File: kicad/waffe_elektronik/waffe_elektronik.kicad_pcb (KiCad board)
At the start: 4 copper layers, 59.6 x 55 mm, 86 parts, among them J1 WS2812 HP-Streifen, J2 GX16 7-polig, J3 USB-C (Flashen + Laden), J4 OLED I²C (Qwiic), J5 Drehgeber, J6 IR-LED + TSOP 6, J7 TF-018, J8 Abzug + Nachladen, M1 Vibromotor, Q1 AO3400A, Q2 AO3400A, Q3 FS8205A, Q4 2N7002, SW3 RESET, SW4 BOOT, U1 IP5306-I2C, U12 USBLC6-2SC6, U14 ZD35Q1GC-IB, U15 DW01A, U2 AMS1117-3.3, U4 ESP32-S3-WROOM-1-N16R8, U6 MAX98357A

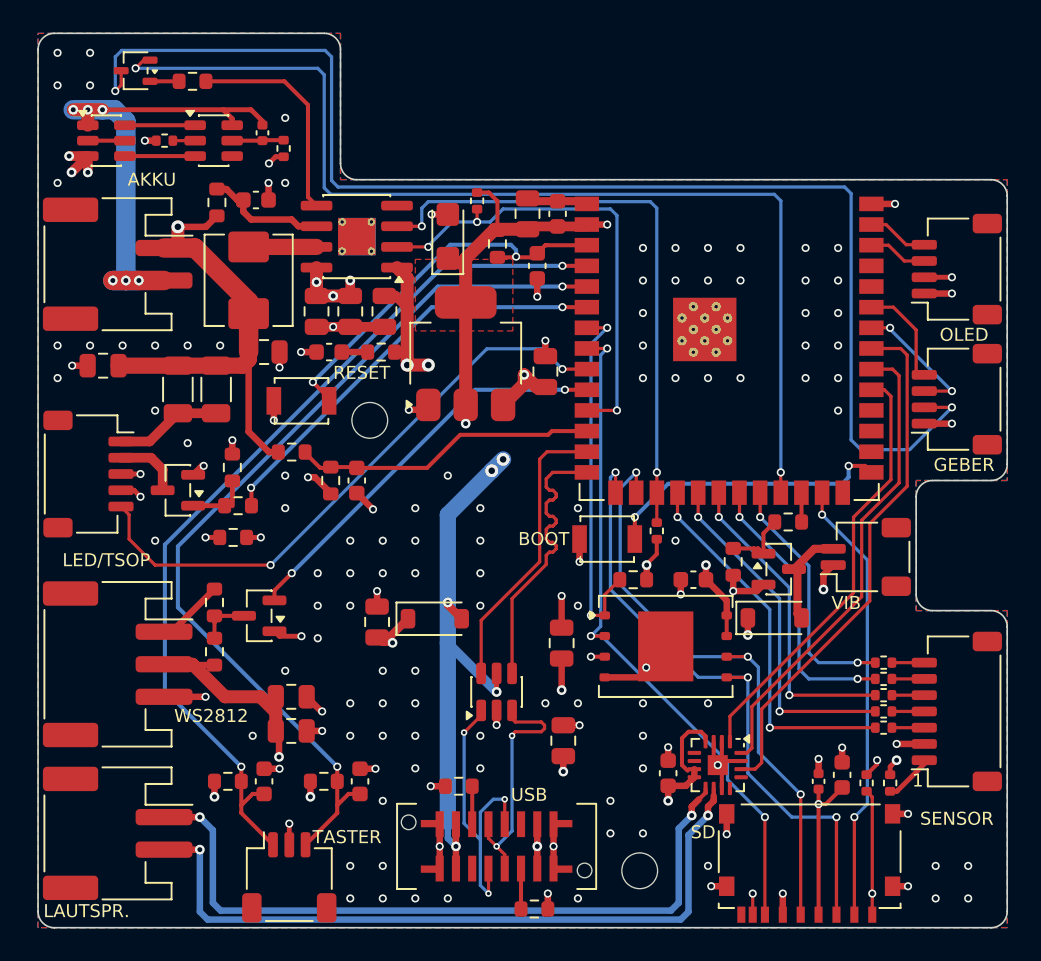
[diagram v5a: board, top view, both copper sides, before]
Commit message: Platine: Lastschalter TPS22810 hinter dem IP5306 (EN = IRQ), RESET in die Lasche, Dämpfung an der USB-Buchse
Co-Authored-By: Claude Opus 5.5 <noreply@anthropic.com>
Claude-Session: https://claude.ai/code/session_01KkZzubjLKyW9odUwvmxTog
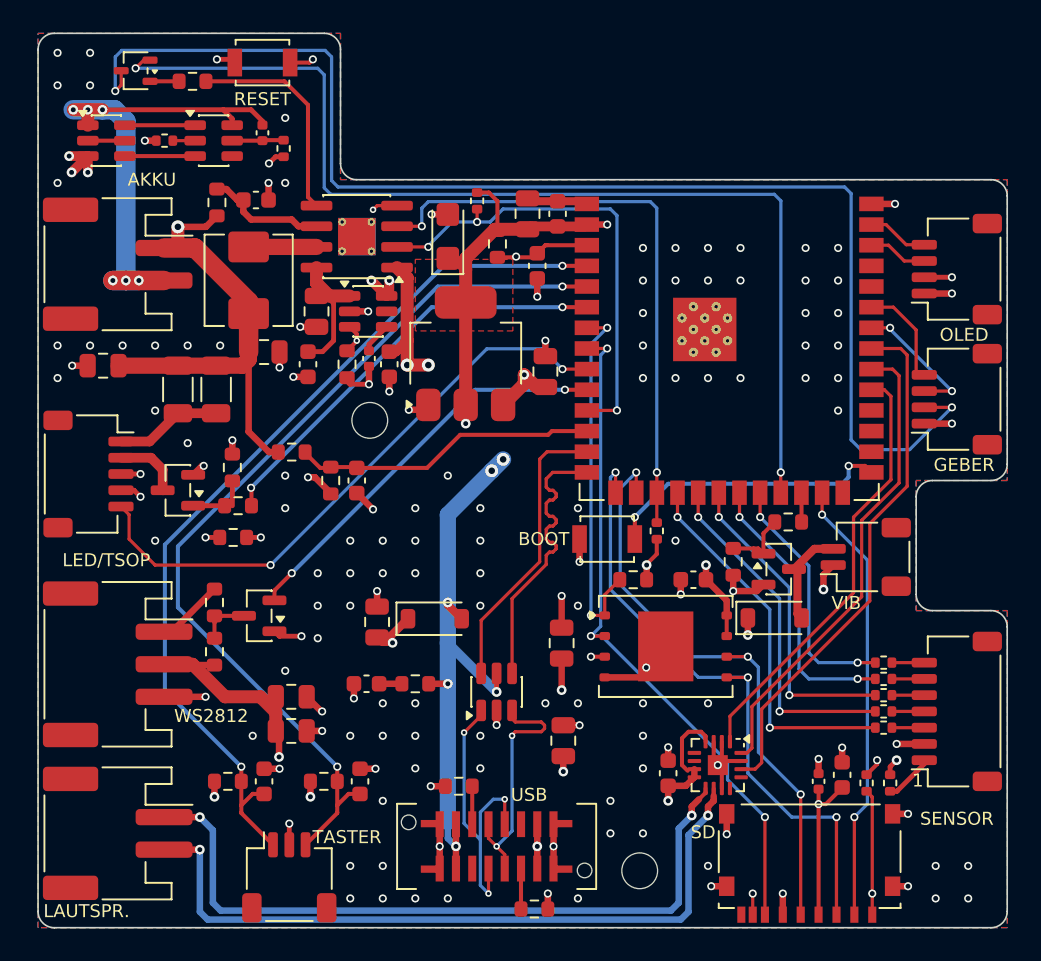
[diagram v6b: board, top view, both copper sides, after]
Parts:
- added C33: 10n, Capacitor_SMD:C_0402_1005Metric, F.Cu at (20.4, 11.0)
- added R42: 100k, Resistor_SMD:R_0603_1608Metric, F.Cu at (19.0, 11.3)
- added U16: TPS22810, Package_TO_SOT_SMD:SOT-23-6, F.Cu at (20.3, 8.10)
- C30: value 22u -> 10u; footprint Capacitor_SMD:C_0805_2012Metric -> Capacitor_SMD:C_0603_1608Metric
- C4: footprint Capacitor_SMD:C_0805_2012Metric -> Capacitor_SMD:C_0603_1608Metric
- moved SW3 20.9 mm to (13.8, -7.20)
- moved C29 20.5 mm to (20.2, 31.0)
- moved R1 20.5 mm to (23.2, 31.0)
- moved C30 4.16 mm to (16.6, 11.3)
- moved C4 3.26 mm to (21.6, 11.3)
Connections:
- C20 pad 1: 5V_PERIPH -> Net-(U1-VOUT)
- C30 pad 1: 5V_PERIPH -> Net-(U1-VOUT)
- U1 pad 4: unconnected-(U1-LED3-Pad4) -> IP_IRQ
- U1 pad 8: 5V_PERIPH -> Net-(U1-VOUT)
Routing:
- net IP_IRQ: track 0.00 -> 12.3 mm, vias 0 -> 2
- net Net-(U1-VOUT): track 0.00 -> 8.11 mm
- net Net-(U4-EN): track 23.9 -> 31.5 mm
- net 5V_PERIPH: track 127.0 -> 119.9 mm, vias 11 -> 10
- net GND: track 73.6 -> 76.1 mm, vias 148 -> 149
- net Net-(U16-CT): track 0.00 -> 1.92 mm
- net VBUS_NATIVE: track 69.4 -> 69.3 mm, vias 8 -> 9

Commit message: Platine: Herstellerzeichen mit Borg-Würfel unter U2, Schaltplan: Westen-TSOP-Ausgänge auf Steckerseite
Co-Authored-By: Claude Opus 5.5 <noreply@anthropic.com>
Claude-Session: https://claude.ai/code/session_01KkZzubjLKyW9odUwvmxTog
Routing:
- net GND: vias 149 -> 144
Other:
- board text added: "lucas.giesecke.cc"
- board text added: "made by"
